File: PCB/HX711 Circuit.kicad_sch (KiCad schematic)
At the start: 10 parts, among them U1 Hx711

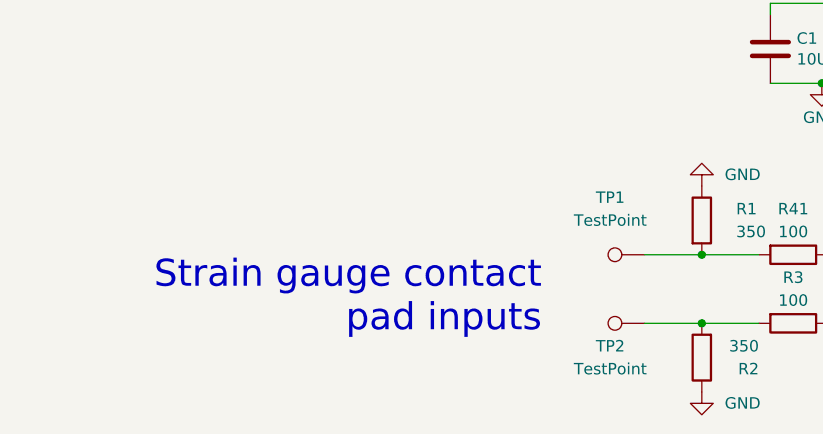
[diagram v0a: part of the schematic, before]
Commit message: Found connector
Found connector, kicad layout and everything else I needed.
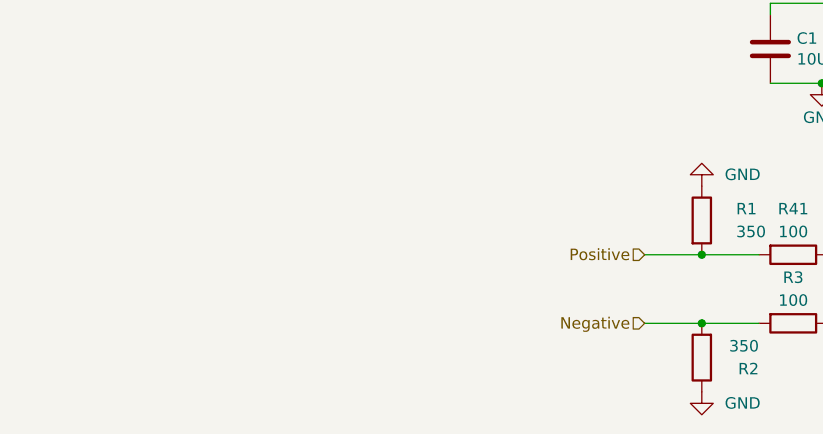
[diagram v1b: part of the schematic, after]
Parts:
- removed TP1, TP2: TestPoint, Custom-footprints:Radial-Pads-With-Relief, symbol Connector:TestPoint
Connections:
- net Positive: now reaches R1.2, R41.2
- net Negative: now reaches R2.2, R3.2
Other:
- note removed: "Strain gauge contact pad inputs"
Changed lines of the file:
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@@
     (stroke (width 0) (type default))
-  )
-  (text "Strain gauge contact \npad inputs\n" (at 96.52 113.03 0)
-    (effects (font (size 3 3)) (justify right bottom))
   )
   (text "Output to shift register" (at 182.88 104.14 0)
@@
     (effects (font (size 1.27 1.27)) (justify left))
   )
+  (hierarchical_label "Negative" (shape input) (at 107.95 111.76 180) (fields_autoplaced)
+    (effects (font (size 1.27 1.27)) (justify right))
+  )
+  (hierarchical_label "Positive" (shape input) (at 107.95 104.14 180) (fields_autoplaced)
+    (effects (font (size 1.27 1.27)) (justify right))
+  )
   (symbol (lib_id "PCB-rescue:C-Device") (at 121.92 81.28 0) (unit 1)
     (in_bom yes) (on_board yes) (dnp no)
@@
         (path "/b6270a28-e0d9-4655-a18a-03dbf007b940/6eed81f2-9ea8-4b15-9b25-b30a760a9be7"
           (reference "R50") (unit 1)
-        )
-      )
-    )
-  )
-  (symbol (lib_id "Connector:TestPoint") (at 107.95 111.76 90) (unit 1)
-    (in_bom yes) (on_board yes) (dnp no)
-    (property "Reference" "TP2" (at 104.14 114.3 90)
-      (effects (font (size 1.27 1.27)))
-    )
-    (property "Value" "TestPoint" (at 104.14 116.84 90)
-      (effects (font (size 1.27 1.27)))
-    )
-    (property "Footprint" "Custom-footprints:Radial-Pads-With-Relief" (at 107.95 106.68 0)
-      (effects (font (size 1.27 1.27)) hide)
-    )
-    (property "Datasheet" "~" (at 107.95 106.68 0)
-      (effects (font (size 1.27 1.27)) hide)
-    )
-    (pin "1")
-    (instances
-      (project "PCB"
-        (path "/b6270a28-e0d9-4655-a18a-03dbf007b940/865df6f9-fa66-4b43-929e-1913f975c2d0"
-          (reference "TP2") (unit 1)
-        )
-        (path "/b6270a28-e0d9-4655-a18a-03dbf007b940/348f29cd-068e-4363-9c21-09b34e523a46"
-          (reference "TP7") (unit 1)
-        )
-        (path "/b6270a28-e0d9-4655-a18a-03dbf007b940/55c2d934-244c-44fa-a407-b54a366ca226"
-          (reference "TP11") (unit 1)
-        )
-        (path "/b6270a28-e0d9-4655-a18a-03dbf007b940/08e9dfb0-f6cf-445e-a76d-3f029063dc7e"
-          (reference "TP16") (unit 1)
-        )
-        (path "/b6270a28-e0d9-4655-a18a-03dbf007b940/c3166b72-45ca-4bb3-84d0-d9a7dc830ff6"
-          (reference "TP21") (unit 1)
-        )
-        (path "/b6270a28-e0d9-4655-a18a-03dbf007b940/437b6eb2-c2ed-4592-b41e-b7f1e7300163"
-          (reference "TP26") (unit 1)
-        )
-        (path "/b6270a28-e0d9-4655-a18a-03dbf007b940/0821f14b-d29c-4d59-b007-c0ebd9554832"
-          (reference "TP4") (unit 1)
-        )
-        (path "/b6270a28-e0d9-4655-a18a-03dbf007b940/eababe2a-0ecd-4427-a6f7-2ec75821d4fc"
-          (reference "TP9") (unit 1)
-        )
-        (path "/b6270a28-e0d9-4655-a18a-03dbf007b940/7ce80e6b-d043-4f1b-ad6b-3c069ab9b9d7"
-          (reference "TP14") (unit 1)
-        )
-        (path "/b6270a28-e0d9-4655-a18a-03dbf007b940/fb1b1fbb-996e-4607-8c6e-29ed755bddb1"
-          (reference "TP18") (unit 1)
-        )
-        (path "/b6270a28-e0d9-4655-a18a-03dbf007b940/570e1fbc-5905-405a-9db3-c7c35f19abe3"
-          (reference "TP23") (unit 1)
-        )
-        (path "/b6270a28-e0d9-4655-a18a-03dbf007b940/6eed81f2-9ea8-4b15-9b25-b30a760a9be7"
-          (reference "TP28") (unit 1)
         )
       )
@@
         )
       )
-    )
-  )
-  (symbol (lib_id "Connector:TestPoint") (at 107.95 104.14 90) (unit 1)
-    (in_bom yes) (on_board yes) (dnp no)
-    (property "Reference" "TP1" (at 104.14 97.79 90)
-      (effects (font (size 1.27 1.27)))
-    )
-    (property "Value" "TestPoint" (at 104.14 100.33 90)
-      (effects (font (size 1.27 1.27)))
-    )
-    (property "Footprint" "Custom-footprints:Radial-Pads-With-Relief" (at 107.95 99.06 0)
-      (effects (font (size 1.27 1.27)) hide)
-    )
-    (property "Datasheet" "~" (at 107.95 99.06 0)
-      (effects (font (size 1.27 1.27)) hide)
-    )
-    (pin "1")
-    (instances
-      (project "PCB"
-        (path "/b6270a28-e0d9-4655-a18a-03dbf007b940/865df6f9-fa66-4b43-929e-1913f975c2d0"
-          (reference "TP1") (unit 1)
-        )
-        (path "/b6270a28-e0d9-4655-a18a-03dbf007b940/348f29cd-068e-4363-9c21-09b34e523a46"
-          (reference "TP6") (unit 1)
-        )
-        (path "/b6270a28-e0d9-4655-a18a-03dbf007b940/55c2d934-244c-44fa-a407-b54a366ca226"
-          (reference "TP10") (unit 1)
-        )
-        (path "/b6270a28-e0d9-4655-a18a-03dbf007b940/08e9dfb0-f6cf-445e-a76d-3f029063dc7e"
-          (reference "TP15") (unit 1)
-        )
-        (path "/b6270a28-e0d9-4655-a18a-03dbf007b940/c3166b72-45ca-4bb3-84d0-d9a7dc830ff6"
-          (reference "TP20") (unit 1)
-        )
-        (path "/b6270a28-e0d9-4655-a18a-03dbf007b940/437b6eb2-c2ed-4592-b41e-b7f1e7300163"
-          (reference "TP25") (unit 1)
-        )
-        (path "/b6270a28-e0d9-4655-a18a-03dbf007b940/0821f14b-d29c-4d59-b007-c0ebd9554832"
-          (reference "TP3") (unit 1)
-        )
-        (path "/b6270a28-e0d9-4655-a18a-03dbf007b940/eababe2a-0ecd-4427-a6f7-2ec75821d4fc"
-          (reference "TP8") (unit 1)
-        )
-        (path "/b6270a28-e0d9-4655-a18a-03dbf007b940/7ce80e6b-d043-4f1b-ad6b-3c069ab9b9d7"
-          (reference "TP13") (unit 1)
-        )
-        (path "/b6270a28-e0d9-4655-a18a-03dbf007b940/fb1b1fbb-996e-4607-8c6e-29ed755bddb1"
-          (reference "TP17") (unit 1)
-        )
-        (path "/b6270a28-e0d9-4655-a18a-03dbf007b940/570e1fbc-5905-405a-9db3-c7c35f19abe3"
-          (reference "TP22") (unit 1)
-        )
-        (path "/b6270a28-e0d9-4655-a18a-03dbf007b940/6eed81f2-9ea8-4b15-9b25-b30a760a9be7"
-          (reference "TP27") (unit 1)
-        )
-      )

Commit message: Changed size of pcb
PCB size increased by 725 square mm by increasing size to a 75 mm by 75 mm square. Dout and the clock for the hx711s have been wired as well as the control wires for the shift registers.
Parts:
- C1, C2, C28: footprint Capacitor_SMD:C_0805_2012Metric_Pad1.18x1.45mm_HandSolder -> Capacitor_SMD:C_0603_1608Metric_Pad1.08x0.95mm_HandSolder
- R1, R2, R3, R41: footprint Resistor_SMD:R_0805_2012Metric_Pad1.20x1.40mm_HandSolder -> Resistor_SMD:R_0603_1608Metric_Pad0.98x0.95mm_HandSolder
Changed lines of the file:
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@@
 			)
 		)
-		(property "Footprint" "Capacitor_SMD:C_0805_2012Metric_Pad1.18x1.45mm_HandSolder"
+		(property "Footprint" "Capacitor_SMD:C_0603_1608Metric_Pad1.08x0.95mm_HandSolder"
 			(at 122.8852 85.09 0)
 			(effects
@@
 			)
 		)
-		(property "Footprint" "Capacitor_SMD:C_0805_2012Metric_Pad1.18x1.45mm_HandSolder"
+		(property "Footprint" "Capacitor_SMD:C_0603_1608Metric_Pad1.08x0.95mm_HandSolder"
 			(at 134.3152 85.09 0)
 			(effects
@@
 			)
 		)
-		(property "Footprint" "Resistor_SMD:R_0805_2012Metric_Pad1.20x1.40mm_HandSolder"
+		(property "Footprint" "Resistor_SMD:R_0603_1608Metric_Pad0.98x0.95mm_HandSolder"
 			(at 124.46 102.362 90)
 			(effects
@@
 			)
 		)
-		(property "Footprint" "Resistor_SMD:R_0805_2012Metric_Pad1.20x1.40mm_HandSolder"
+		(property "Footprint" "Resistor_SMD:R_0603_1608Metric_Pad0.98x0.95mm_HandSolder"
 			(at 112.522 100.33 90)
 			(effects
@@
 			)
 		)
-		(property "Footprint" "Resistor_SMD:R_0805_2012Metric_Pad1.20x1.40mm_HandSolder"
+		(property "Footprint" "Resistor_SMD:R_0603_1608Metric_Pad0.98x0.95mm_HandSolder"
 			(at 124.46 109.982 90)
 			(effects
@@
 			)
 		)
-		(property "Footprint" "Resistor_SMD:R_0805_2012Metric_Pad1.20x1.40mm_HandSolder"
+		(property "Footprint" "Resistor_SMD:R_0603_1608Metric_Pad0.98x0.95mm_HandSolder"
 			(at 116.078 115.57 90)
 			(effects
@@
 			)
 		)
-		(property "Footprint" "Capacitor_SMD:C_0805_2012Metric_Pad1.18x1.45mm_HandSolder"
+		(property "Footprint" "Capacitor_SMD:C_0603_1608Metric_Pad1.08x0.95mm_HandSolder"
 			(at 131.7752 111.76 0)
 			(effects

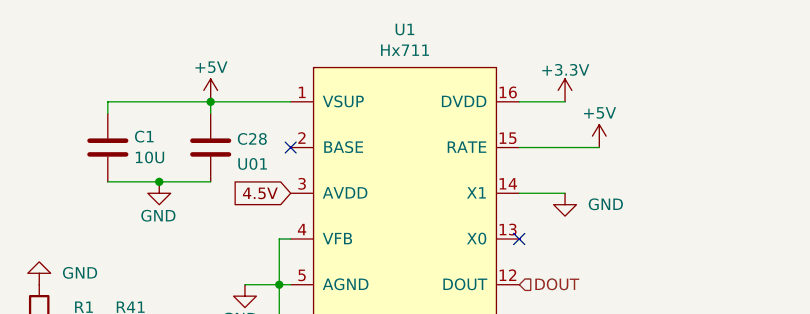
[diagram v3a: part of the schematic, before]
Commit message: Added test points and changed labels
Added test points for nearly every single cable. Labels on individual sections changed to better reflect the actual board.
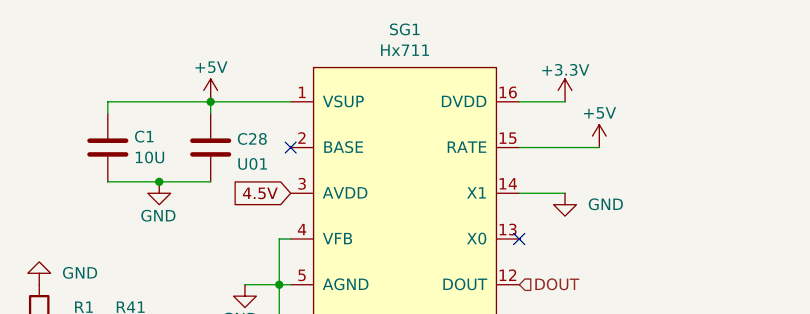
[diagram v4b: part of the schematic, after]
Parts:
- renumbered U1 to SG1
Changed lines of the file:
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@@
 		(on_board yes)
 		(dnp no)
-		(property "Reference" "U1"
+		(property "Reference" "SG1"
 			(at 154.94 68.199 0)
 			(effects
@@
 			(project "PCB"
 				(path "/b6270a28-e0d9-4655-a18a-03dbf007b940/865df6f9-fa66-4b43-929e-1913f975c2d0"
-					(reference "U1")
+					(reference "SG1")
 					(unit 1)
 				)
 				(path "/b6270a28-e0d9-4655-a18a-03dbf007b940/348f29cd-068e-4363-9c21-09b34e523a46"
-					(reference "U3")
+					(reference "SG3")
 					(unit 1)
 				)
 				(path "/b6270a28-e0d9-4655-a18a-03dbf007b940/55c2d934-244c-44fa-a407-b54a366ca226"
-					(reference "U5")
+					(reference "SG5")
 					(unit 1)
 				)
 				(path "/b6270a28-e0d9-4655-a18a-03dbf007b940/08e9dfb0-f6cf-445e-a76d-3f029063dc7e"
-					(reference "U7")
+					(reference "SG7")
 					(unit 1)
 				)
 				(path "/b6270a28-e0d9-4655-a18a-03dbf007b940/c3166b72-45ca-4bb3-84d0-d9a7dc830ff6"
-					(reference "U9")
+					(reference "SG9")
 					(unit 1)
 				)
 				(path "/b6270a28-e0d9-4655-a18a-03dbf007b940/437b6eb2-c2ed-4592-b41e-b7f1e7300163"
-					(reference "U11")
+					(reference "SG11")
 					(unit 1)
 				)
 				(path "/b6270a28-e0d9-4655-a18a-03dbf007b940/0821f14b-d29c-4d59-b007-c0ebd9554832"
-					(reference "U2")
+					(reference "SG2")
 					(unit 1)
 				)
 				(path "/b6270a28-e0d9-4655-a18a-03dbf007b940/eababe2a-0ecd-4427-a6f7-2ec75821d4fc"
-					(reference "U4")
+					(reference "SG4")
 					(unit 1)
 				)
 				(path "/b6270a28-e0d9-4655-a18a-03dbf007b940/7ce80e6b-d043-4f1b-ad6b-3c069ab9b9d7"
-					(reference "U6")
+					(reference "SG6")
 					(unit 1)
 				)
 				(path "/b6270a28-e0d9-4655-a18a-03dbf007b940/fb1b1fbb-996e-4607-8c6e-29ed755bddb1"
-					(reference "U8")
+					(reference "SG8")
 					(unit 1)
 				)
 				(path "/b6270a28-e0d9-4655-a18a-03dbf007b940/570e1fbc-5905-405a-9db3-c7c35f19abe3"
-					(reference "U10")
+					(reference "SG10")
 					(unit 1)
 				)
 				(path "/b6270a28-e0d9-4655-a18a-03dbf007b940/6eed81f2-9ea8-4b15-9b25-b30a760a9be7"
-					(reference "U12")
+					(reference "SG12")
 					(unit 1)
 				)

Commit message: Silkscreen updated
The strain gauges are correctly labeled now as well as the test points for all individual hx711 amplifiers. All the voltages are completely labeled as well. There are many 4.5V, 5V and 3.3V  test points. Every digital signal has its test point. To place the test points, I replaced some of the vias with test points or spliced two lines together.
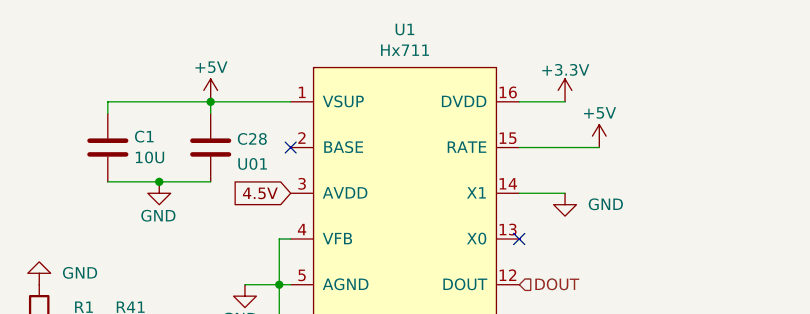
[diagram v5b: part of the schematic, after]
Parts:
- renumbered SG1 to U1
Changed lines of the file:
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@@
 		(on_board yes)
 		(dnp no)
-		(property "Reference" "SG1"
+		(property "Reference" "U1"
 			(at 154.94 68.199 0)
 			(effects
@@
 			(project "PCB"
 				(path "/b6270a28-e0d9-4655-a18a-03dbf007b940/865df6f9-fa66-4b43-929e-1913f975c2d0"
-					(reference "SG1")
+					(reference "U1")
 					(unit 1)
 				)
 				(path "/b6270a28-e0d9-4655-a18a-03dbf007b940/348f29cd-068e-4363-9c21-09b34e523a46"
-					(reference "SG3")
+					(reference "U3")
 					(unit 1)
 				)
 				(path "/b6270a28-e0d9-4655-a18a-03dbf007b940/55c2d934-244c-44fa-a407-b54a366ca226"
-					(reference "SG5")
+					(reference "U5")
 					(unit 1)
 				)
 				(path "/b6270a28-e0d9-4655-a18a-03dbf007b940/08e9dfb0-f6cf-445e-a76d-3f029063dc7e"
-					(reference "SG7")
+					(reference "U7")
 					(unit 1)
 				)
 				(path "/b6270a28-e0d9-4655-a18a-03dbf007b940/c3166b72-45ca-4bb3-84d0-d9a7dc830ff6"
-					(reference "SG9")
+					(reference "U9")
 					(unit 1)
 				)
 				(path "/b6270a28-e0d9-4655-a18a-03dbf007b940/437b6eb2-c2ed-4592-b41e-b7f1e7300163"
-					(reference "SG11")
+					(reference "U11")
 					(unit 1)
 				)
 				(path "/b6270a28-e0d9-4655-a18a-03dbf007b940/0821f14b-d29c-4d59-b007-c0ebd9554832"
-					(reference "SG2")
+					(reference "U2")
 					(unit 1)
 				)
 				(path "/b6270a28-e0d9-4655-a18a-03dbf007b940/eababe2a-0ecd-4427-a6f7-2ec75821d4fc"
-					(reference "SG4")
+					(reference "U4")
 					(unit 1)
 				)
 				(path "/b6270a28-e0d9-4655-a18a-03dbf007b940/7ce80e6b-d043-4f1b-ad6b-3c069ab9b9d7"
-					(reference "SG6")
+					(reference "U6")
 					(unit 1)
 				)
 				(path "/b6270a28-e0d9-4655-a18a-03dbf007b940/fb1b1fbb-996e-4607-8c6e-29ed755bddb1"
-					(reference "SG8")
+					(reference "U8")
 					(unit 1)
 				)
 				(path "/b6270a28-e0d9-4655-a18a-03dbf007b940/570e1fbc-5905-405a-9db3-c7c35f19abe3"
-					(reference "SG10")
+					(reference "U10")
 					(unit 1)
 				)
 				(path "/b6270a28-e0d9-4655-a18a-03dbf007b940/6eed81f2-9ea8-4b15-9b25-b30a760a9be7"
-					(reference "SG12")
+					(reference "U12")
 					(unit 1)
 				)

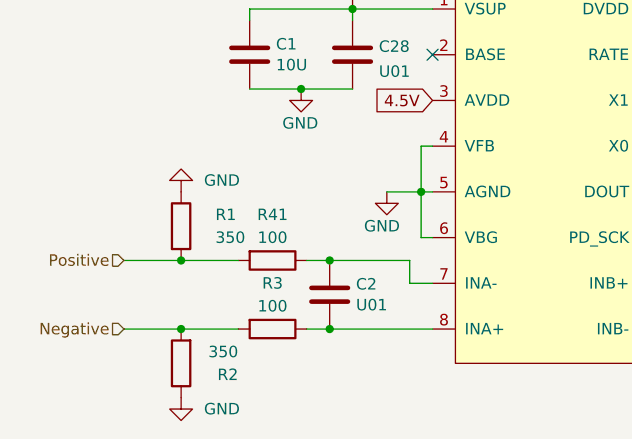
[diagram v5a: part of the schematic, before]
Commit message: Updated gerbers and ready to order
Still need to figure out how to add components to the bill of materials with the digikey part numbers, probably can do that in the descriptions.
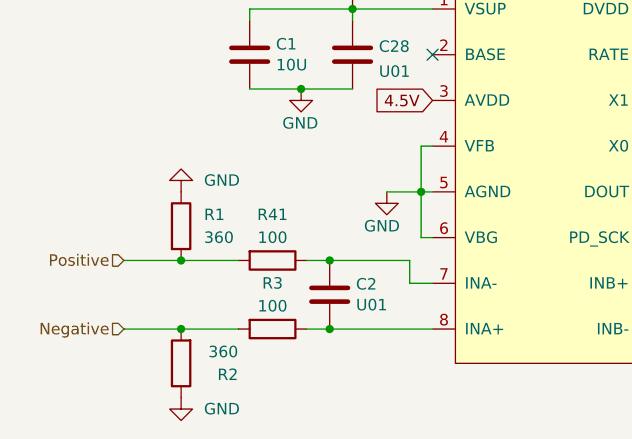
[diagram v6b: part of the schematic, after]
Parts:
- R1, R2: value 350 -> 360
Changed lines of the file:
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@@
 			)
 		)
-		(property "Datasheet" ""
+		(property "Datasheet" "https://mm.digikey.com/Volume0/opasdata/d220001/medias/docus/609/CL10A106MQ8NNNC_Spec.pdf"
 			(at 121.92 81.28 0)
 			(effects
@@
 			)
 		)
-		(property "Datasheet" "~"
+		(property "Datasheet" "https://mm.digikey.com/Volume0/opasdata/d220001/medias/docus/609/CL10A106MQ8NNNC_Spec.pdf"
 			(at 133.35 81.28 0)
 			(effects
@@
 			)
 		)
-		(property "Datasheet" ""
+		(property "Datasheet" "https://www.yageo.com/upload/media/product/products/datasheet/rchip/PYu-RC_Group_51_RoHS_L_12.pdf"
 			(at 124.46 104.14 0)
 			(effects
@@
 		(fields_autoplaced yes)
 		(property "Reference" "R1"
-			(at 118.11 99.0599 0)
+			(at 116.84 99.0599 0)
 			(effects
 				(font
@@
 			)
 		)
-		(property "Value" "350"
-			(at 118.11 101.5999 0)
+		(property "Value" "360"
+			(at 116.84 101.5999 0)
 			(effects
 				(font
@@
 			)
 		)
-		(property "Value" "350"
+		(property "Value" "360"
 			(at 120.65 114.3 0)
 			(effects
@@
 			)
 		)
-		(property "Datasheet" ""
+		(property "Datasheet" "https://mm.digikey.com/Volume0/opasdata/d220001/medias/docus/609/CL10A106MQ8NNNC_Spec.pdf"
 			(at 130.81 107.95 0)
 			(effects
